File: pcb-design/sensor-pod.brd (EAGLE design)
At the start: 79.7 x 125.7 mm, 22 parts, among them X1 PH_SENSOR, X10 I2C_5V, X11 3.3V, X12 3.3V, X15 MB-LEFT, X16 MB-RIGHT, X2 I2C_5V, X3 TURBIDITY, X4 5V, X5 TEMPERATURE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

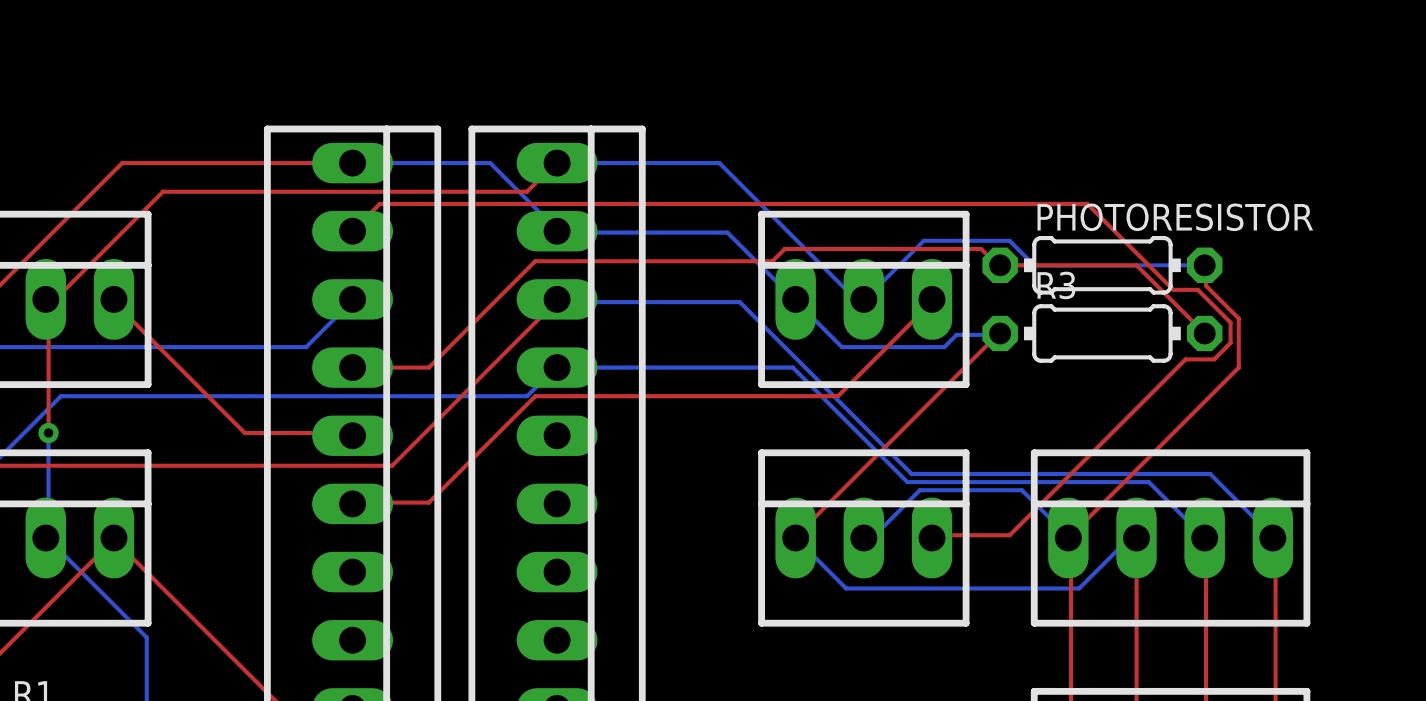
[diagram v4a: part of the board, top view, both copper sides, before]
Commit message: Sensor-pod local temp test.
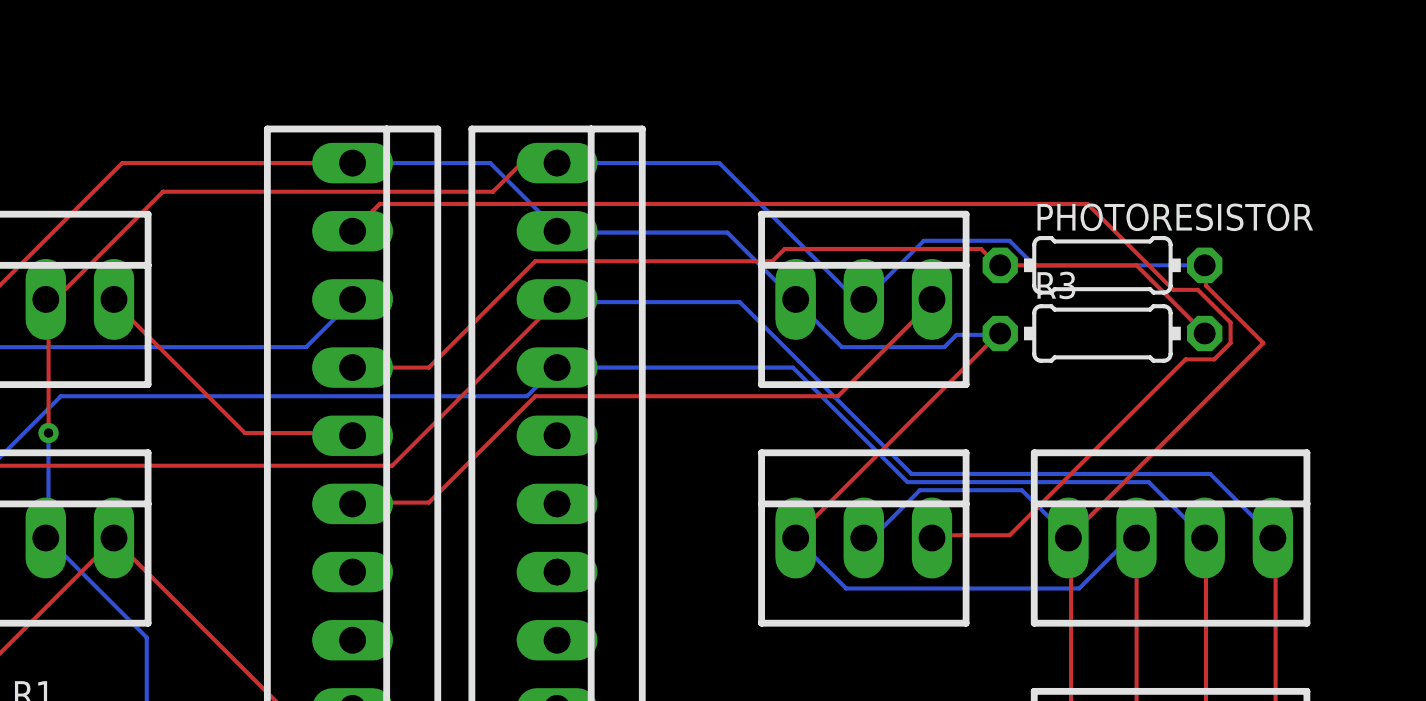
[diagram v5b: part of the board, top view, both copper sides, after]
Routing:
- net 3.3V: track 141.6 -> 142.4 mm
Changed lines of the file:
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@@
 <wire x1="16.6116" y1="33.0708" x2="16.51" y2="33.02" width="0.1524" layer="1"/>
 <wire x1="67.3608" y1="67.818" x2="67.3608" y2="68.58" width="0.1524" layer="1"/>
-<wire x1="68.58" y1="66.5988" x2="67.3608" y2="67.818" width="0.1524" layer="1"/>
-<wire x1="68.58" y1="64.77" x2="68.58" y2="66.5988" width="0.1524" layer="1"/>
-<wire x1="62.23" y1="58.42" x2="68.58" y2="64.77" width="0.1524" layer="1"/>
+<wire x1="69.4944" y1="65.6844" x2="67.3608" y2="67.818" width="0.1524" layer="1"/>
+<wire x1="62.23" y1="58.42" x2="69.4944" y2="65.6844" width="0.1524" layer="1"/>
 <wire x1="67.3608" y1="68.58" x2="67.31" y2="68.58" width="0.1524" layer="1"/>
 <wire x1="55.0164" y1="58.5216" x2="54.7116" y2="58.5216" width="0.1524" layer="16"/>
@@
 <wire x1="24.5364" y1="67.3608" x2="24.2316" y2="67.3608" width="0.1524" layer="1"/>
 <wire x1="28.4988" y1="71.3232" x2="24.5364" y2="67.3608" width="0.1524" layer="1"/>
-<wire x1="42.0624" y1="71.3232" x2="28.4988" y2="71.3232" width="0.1524" layer="1"/>
-<wire x1="43.1292" y1="72.39" x2="42.0624" y2="71.3232" width="0.1524" layer="1"/>
+<wire x1="40.7924" y1="71.3232" x2="28.4988" y2="71.3232" width="0.1524" layer="1"/>
+<wire x1="41.8592" y1="72.39" x2="40.7924" y2="71.3232" width="0.1524" layer="1"/>
 <wire x1="24.2316" y1="67.3608" x2="24.13" y2="67.31" width="0.1524" layer="1"/>
-<wire x1="43.1292" y1="72.39" x2="43.18" y2="72.39" width="0.1524" layer="1"/>
+<wire x1="41.8592" y1="72.39" x2="43.18" y2="72.39" width="0.1524" layer="1"/>
 <wire x1="54.2544" y1="67.3608" x2="54.5592" y2="67.3608" width="0.1524" layer="16"/>
 <wire x1="49.2252" y1="72.39" x2="54.2544" y2="67.3608" width="0.1524" layer="16"/>
